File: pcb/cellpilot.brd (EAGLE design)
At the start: 63 x 54.5 mm, 26 parts, among them IC1 STM32F10XCXT6, K1 PIN20X2, U1 EEPROM-I2CSMD

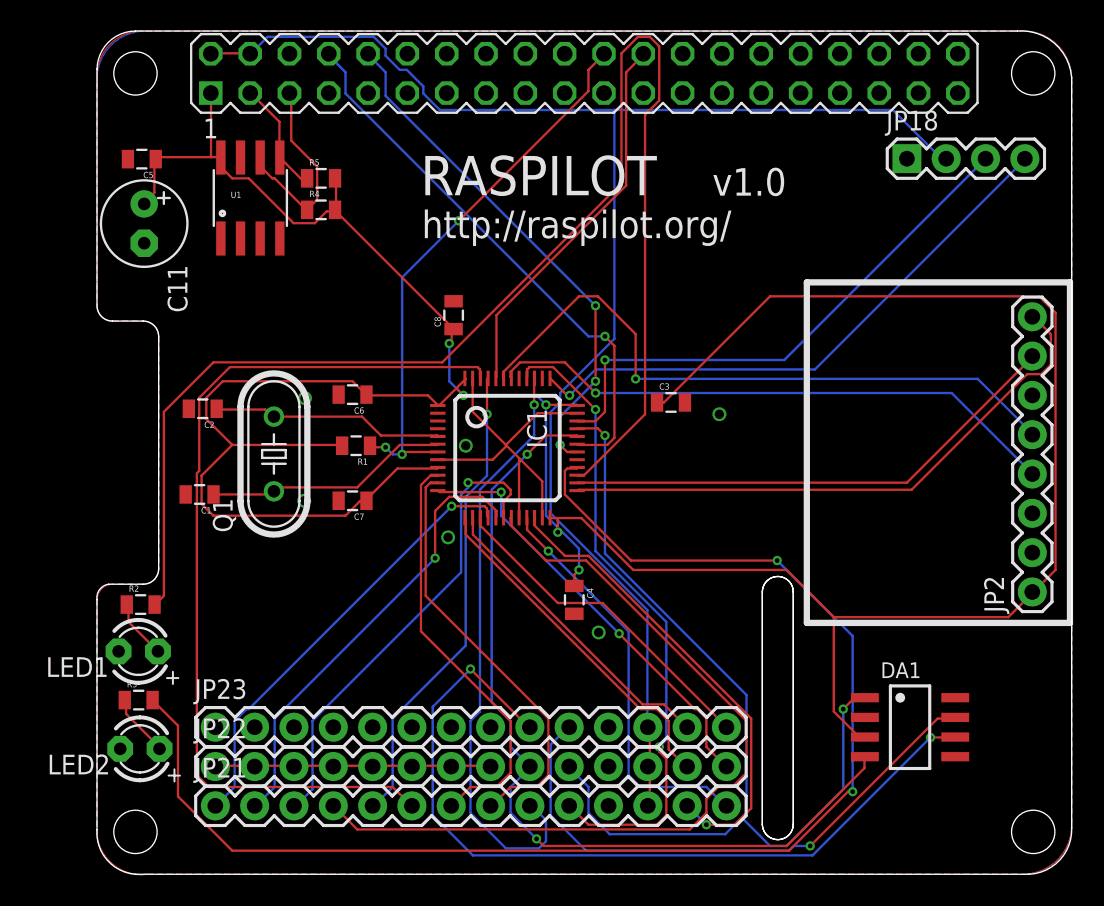
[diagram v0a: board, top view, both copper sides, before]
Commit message: move connector
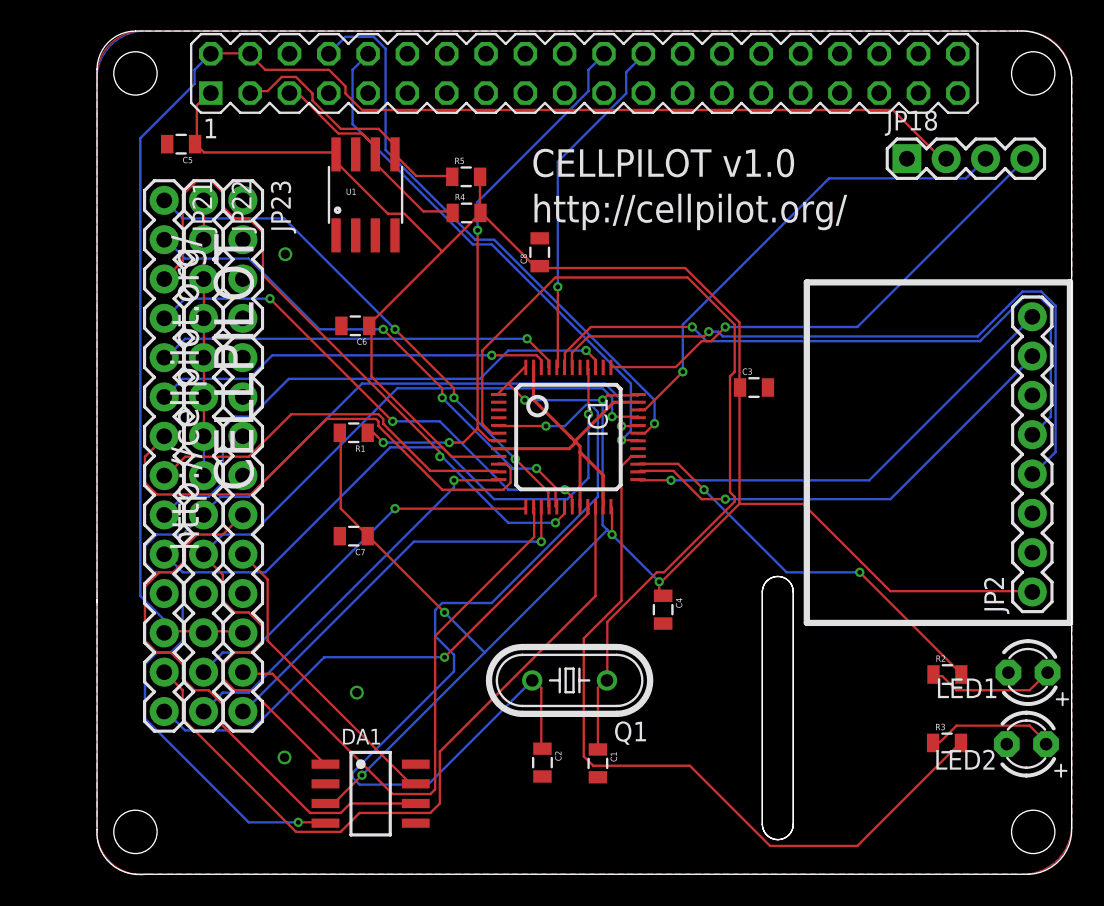
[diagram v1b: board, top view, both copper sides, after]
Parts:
- removed C11: (no value), adafruit:E2,5-6
- moved LED1 57.5 mm to (61.2, 13.8)
- moved LED2 57.3 mm to (61.1, 9.17)
- moved R2 52.3 mm to (56.0, 13.7)
- moved R3 52.3 mm to (55.9, 9.25)
- moved JP21 39.3 mm to (5.36, 44.3), turned to 270 degrees
- moved JP22 36.6 mm to (7.90, 44.3), turned to 270 degrees
- moved DA1 35.1 mm to (18.7, 5.97)
- moved JP23 34.1 mm to (10.4, 44.3), turned to 270 degrees
- moved C2 31.7 mm to (29.8, 7.98), turned to 270 degrees
- moved C1 31.0 mm to (33.4, 7.92), turned to 270 degrees
- moved Q1 24.1 mm to (31.5, 13.3), turned to 180 degrees
- moved R4 9.40 mm to (24.9, 43.5)
- moved R5 9.37 mm to (24.9, 45.8)
- moved U1 7.44 mm to (18.4, 44.7)
- moved C8 6.89 mm to (29.6, 40.9)
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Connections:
- net +3V3: no longer C11.+
- net GND: no longer C11.-
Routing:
- net LED1: track 90.1 -> 26.5 mm, vias 0 -> 2
- net OSC1: track 15.0 -> 59.6 mm, vias 0 -> 1
- net OSC2: track 15.9 -> 57.2 mm
- net LED2: track 88.4 -> 50.6 mm, vias 2 -> 0
- net PWM6: track 58.8 -> 26.1 mm, vias 0 -> 1
- net +3V3: track 203.6 -> 180.7 mm, vias 5 -> 6
- net PWM4: track 53.7 -> 32.8 mm, vias 0 -> 3
- net CAN_L: track 53.9 -> 36.0 mm, vias 2 -> 0
- net CAN_H: track 36.9 -> 19.6 mm, vias 1 -> 0
- net USART3_RX: track 30.6 -> 47.2 mm, vias 1 -> 0
- net PM_V: track 20.1 -> 36.7 mm
- net PWM3: track 30.5 -> 43.2 mm, vias 1 -> 2
- net CAN_RX: track 56.0 -> 67.2 mm
- net EEPROM_SDA: track 7.30 -> 16.8 mm
- net SCL: track 37.4 -> 46.0 mm
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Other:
- outline, holes or cut-outs redrawn
- board text added: "CELLPILOT"
- board text added: "CELLPILOT v1.0"
- board text added: "http://cellpilot.org/"
- board text removed: "RASPILOT"
- board text removed: "http://raspilot.org/"
- board text removed: "v1.0"
